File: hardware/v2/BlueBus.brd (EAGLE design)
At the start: 95 x 65 mm, 143 parts, among them J1 3PIN_953442_1, J2 6PIN_953442_1, J3 6PIN_5_103166_1, J4 SJ2-35853A-SMT-TR, J5 SMB_CONN, J6 USB3080-30-01-A, J7 PCM12SMTR, J8 TC2030NL, Q1 NMOSFET-BSS138K, Q2 NMOSFET-BSS138K, Q3 PMOSFET-DMP32D4SSOT323, U1 MPQ4420, U10 PCM5122, U11 PAM8406, U2 TH3122.4, U3 FT231XS, U4 S-1212BC0-U5T1U, U5 XC6210, U6 CAT25M01, U7 PIC24FJ1024GA606, U8 BM83SM1, U9 DIT4096

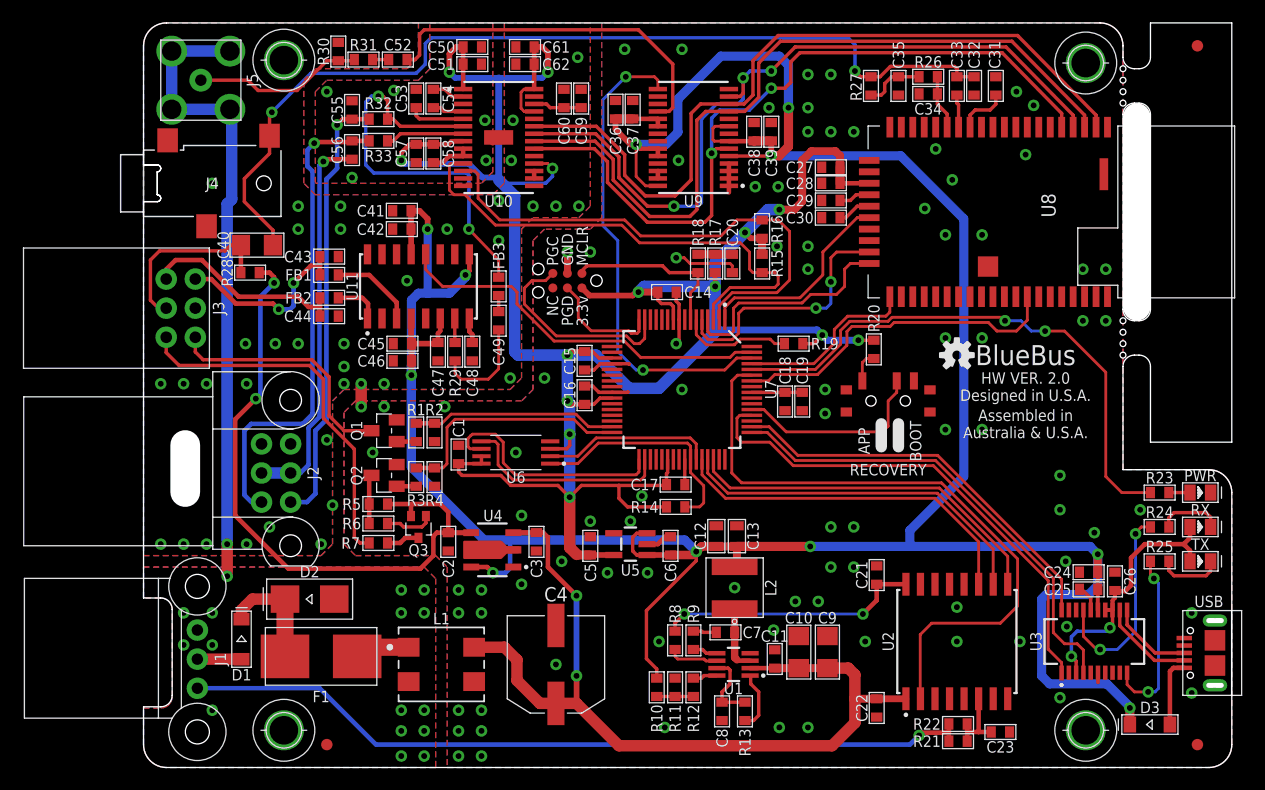
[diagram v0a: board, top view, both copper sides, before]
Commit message: [IMP] hardware: v2 Hardware updates for manufacture * Remove USB cutout * Swap PTH holes to simple holes * Add tCream to USB mount holes
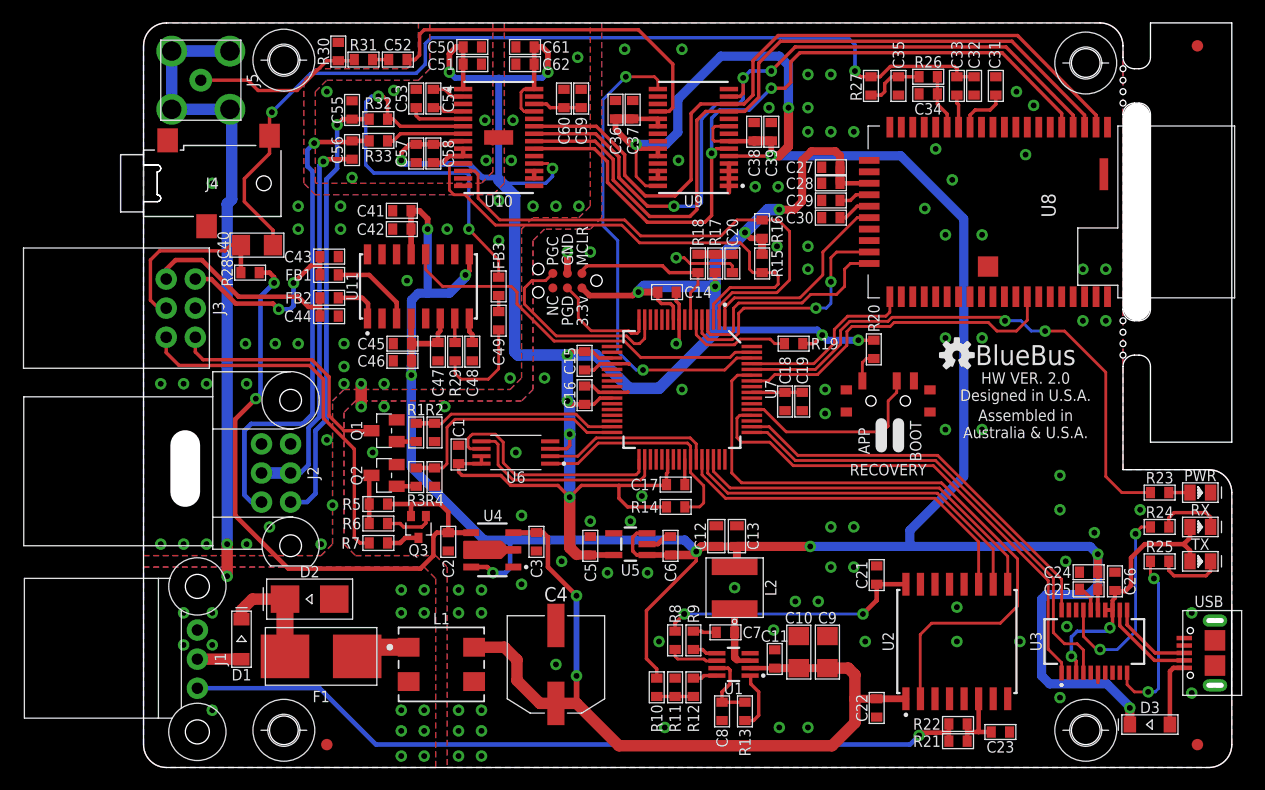
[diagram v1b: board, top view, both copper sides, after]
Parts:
- H1, H2, H3, H4: value 2,5-PAD -> 2,5-HOLE; device Connectors:2.5-PAD -> Connectors:2.5-HOLE
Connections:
- net GND: no longer H2.B2,5, H3.B2,5, H4.B2,5
- net GND_FLT: no longer H1.B2,5
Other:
- outline, holes or cut-outs redrawn
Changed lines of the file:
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@@
 <text x="38.3" y="43.8" size="1" layer="25" font="vector" ratio="15" rot="R90" align="center-left">MCLR</text>
 <text x="37" y="43.8" size="1" layer="25" font="vector" ratio="15" rot="R90" align="center-left">GND</text>
-<wire x1="0" y1="14.8" x2="1.5" y2="14.8" width="0" layer="20"/>
-<wire x1="1.5" y1="14.8" x2="2.5" y2="13.8" width="0" layer="20" curve="-90"/>
-<wire x1="2.5" y1="13.8" x2="2.5" y2="6.3" width="0" layer="20"/>
-<wire x1="2.5" y1="6.3" x2="1.5" y2="5.3" width="0" layer="20" curve="-90"/>
-<wire x1="1.5" y1="5.3" x2="0" y2="5.3" width="0" layer="20"/>
 <wire x1="64.4" y1="30" x2="64.4" y2="28" width="1" layer="25"/>
 <wire x1="65.9" y1="30" x2="65.9" y2="28" width="1" layer="25"/>
@@
 <wire x1="19.85" y1="38.85" x2="5.65" y2="38.85" width="0.1" layer="26"/>
 <wire x1="5.65" y1="41.3" x2="19.85" y2="41.3" width="0.1" layer="26"/>
+<wire x1="0" y1="5.3" x2="0" y2="14.8" width="0" layer="20"/>
 </plain>
 <attributes>
@@
 <attribute name="PN" value="FT231XS-R" x="83" y="11" size="1.778" layer="27" display="off"/>
 </element>
-<element name="H1" library="Connectors" package="2.5-PAD" value="2,5-PAD" x="12.25" y="3.25" smashed="yes"/>
-<element name="H2" library="Connectors" package="2.5-PAD" value="2,5-PAD" x="12.25" y="61.75" smashed="yes"/>
-<element name="H3" library="Connectors" package="2.5-PAD" value="2,5-PAD" x="82.25" y="61.5" smashed="yes"/>
-<element name="H4" library="Connectors" package="2.5-PAD" value="2,5-PAD" x="82.25" y="3.25" smashed="yes"/>
+<element name="H1" library="Connectors" package="2.5-HOLE" value="2,5-HOLE" x="12.25" y="3.25" smashed="yes"/>
+<element name="H2" library="Connectors" package="2.5-HOLE" value="2,5-HOLE" x="12.25" y="61.75" smashed="yes"/>
+<element name="H3" library="Connectors" package="2.5-HOLE" value="2,5-HOLE" x="82.25" y="61.5" smashed="yes"/>
+<element name="H4" library="Connectors" package="2.5-HOLE" value="2,5-HOLE" x="82.25" y="3.25" smashed="yes"/>
 <element name="L2" library="Passives" package="MPL-SE5040" value="10uH" x="51.6" y="15.7" smashed="yes" rot="R270">
 <attribute name="MFG" value="Monolithic Power Systems" x="-10.63" y="-30.02" size="1.778" layer="27" rot="R270" display="off"/>
@@
 <contactref element="C6" pad="2"/>
 <contactref element="J3" pad="4"/>
-<contactref element="H2" pad="B2,5"/>
-<contactref element="H3" pad="B2,5"/>
-<contactref element="H4" pad="B2,5"/>
 <contactref element="C8" pad="2"/>
 <contactref element="C10" pad="2"/>
@@
 <contactref element="J1" pad="1"/>
 <contactref element="L1" pad="2"/>
-<contactref element="H1" pad="B2,5"/>
 <via x="22.5" y="15.5" extent="1-16" drill="0.51"/>
 <via x="24.5" y="15.5" extent="1-16" drill="0.51"/>
@@
 <vertex x="2" y="0" curve="-90"/>
 <vertex x="0" y="2"/>
-<vertex x="0" y="5.2"/>
-<vertex x="1.5" y="5.2" curve="90"/>
-<vertex x="2.5" y="6.2"/>
-<vertex x="2.5" y="13.8" curve="90"/>
-<vertex x="1.5" y="14.8"/>
 <vertex x="0" y="14.8"/>
 <vertex x="0" y="17.5"/>
@@
 <vertex x="2" y="0" curve="-90"/>
 <vertex x="0" y="2"/>
-<vertex x="0" y="5.2"/>
-<vertex x="1.5" y="5.2" curve="90"/>
-<vertex x="2.5" y="6.2"/>
-<vertex x="2.5" y="13.8" curve="90"/>
-<vertex x="1.5" y="14.8"/>
 <vertex x="0" y="14.8"/>
 <vertex x="0" y="17.5"/>

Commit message: [IMP] harcware: Hardware version 2.1 * Swap U4/S-1212BC0 for SOT23-5 package * Update resistor value for R19 to resolve bug with board version identification
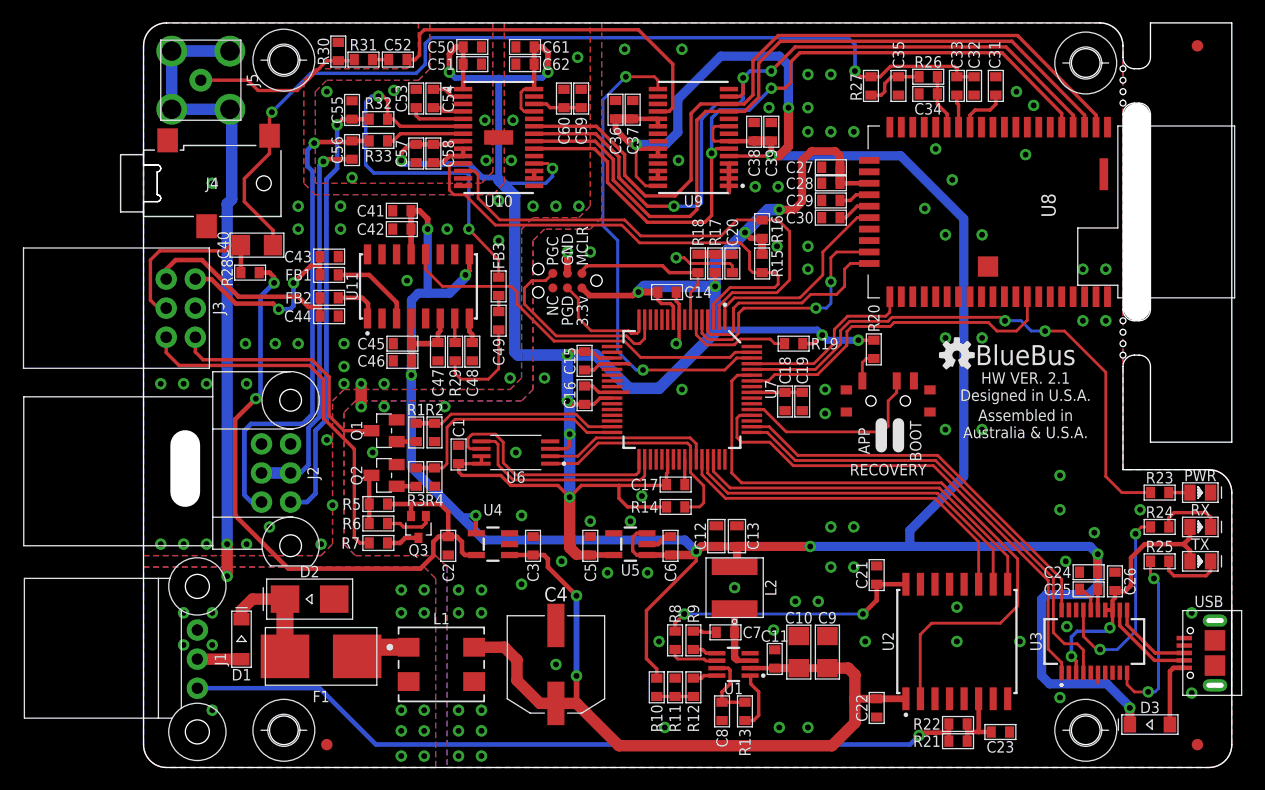
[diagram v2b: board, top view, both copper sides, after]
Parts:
- R19: value 10k -> 100
- U4: value S-1212BC0-U5T1U -> S-1212BC0-M5T1U; device ICs:SOT-89-5 -> ICs:SOT23-5
- moved U4 0.50 mm to (30.5, 19.5)
- moved C3 0.46 mm to (34.0, 19.4), turned to 90 degrees
- moved C2 0.35 mm to (26.6, 19.4)
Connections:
- net 12V: now also U4.5; no longer U4.4
- net 5V: now also U4.4; no longer U4.5
- net VIN: now also U4.1; no longer U4.3
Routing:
- net 5V: track 272.3 -> 269.1 mm
- net VIN: track 75.4 -> 73.9 mm
- net 12V: track 57.0 -> 58.5 mm
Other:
- outline, holes or cut-outs redrawn
- board text added: "HW VER. 2.1"
- board text removed: "HW VER. 2.0"

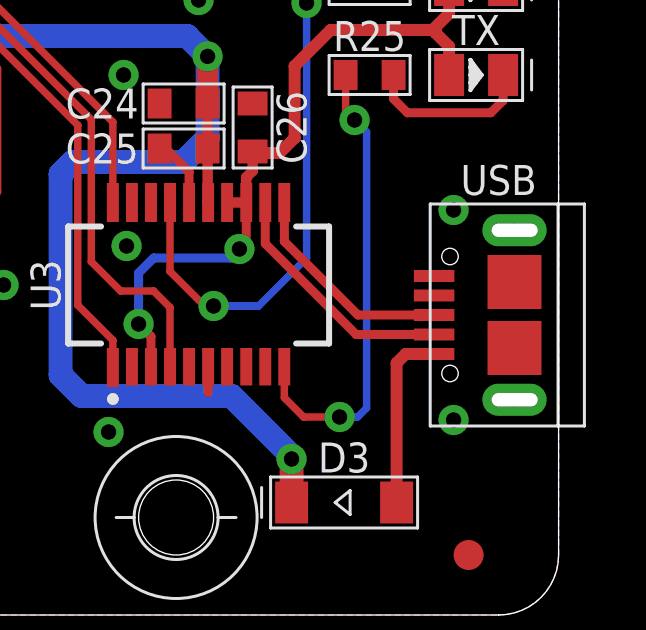
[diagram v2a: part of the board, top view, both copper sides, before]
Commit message: [IMP] hardware: Minor updates to v2.1 * Update EEPROM P/N * Update U6 text layer on PCB * Increase USB port locating pin drill size to 0.65mm to prevent PNP issues
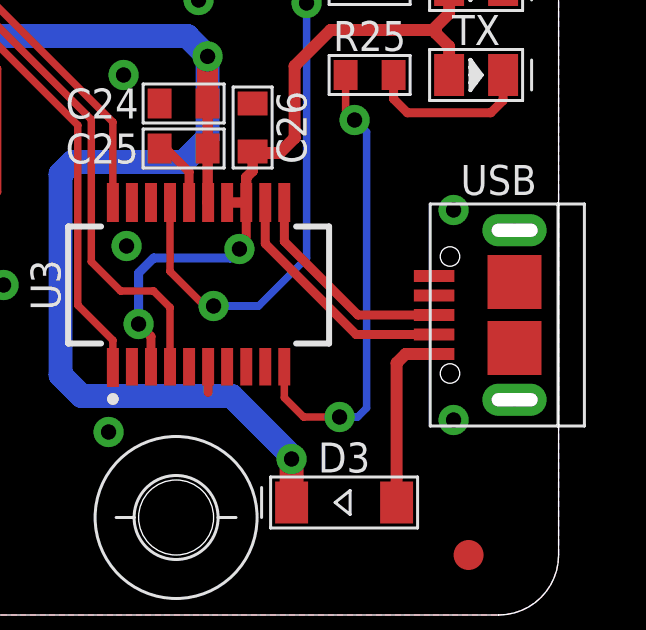
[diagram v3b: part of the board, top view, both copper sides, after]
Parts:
- U6: value CAT25M01 -> CAT25128
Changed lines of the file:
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@@
 <attribute name="PN" value="DIT4096IPW" x="48" y="55" size="1.778" layer="27" rot="R180" display="off"/>
 </element>
-<element name="U6" library="ICs" package="TSSOP-8" value="CAT25M01" x="32.5" y="27.5" smashed="yes" rot="R180">
+<element name="U6" library="ICs" package="TSSOP-8" value="CAT25128" x="32.5" y="27.5" smashed="yes" rot="R180">
 <attribute name="MFG" value="ONSEMI" x="32.5" y="27.5" size="1.778" layer="27" rot="R180" display="off"/>
-<attribute name="NAME" x="32.5" y="25.85" size="1" layer="21" font="vector" ratio="15" rot="R180" align="bottom-center"/>
-<attribute name="PN" value="CAT25M01YI-GT3" x="32.5" y="27.5" size="1.778" layer="27" rot="R180" display="off"/>
+<attribute name="NAME" x="32.5" y="25.85" size="1" layer="25" font="vector" ratio="15" rot="R180" align="bottom-center"/>
+<attribute name="PN" value="CAT25128YI-GT3" x="32.5" y="27.5" size="1.778" layer="27" rot="R180" display="off"/>
 </element>
 <element name="C38" library="Passives" package="0603" value="0.1uF" x="53.3" y="55.5" smashed="yes" rot="R90">

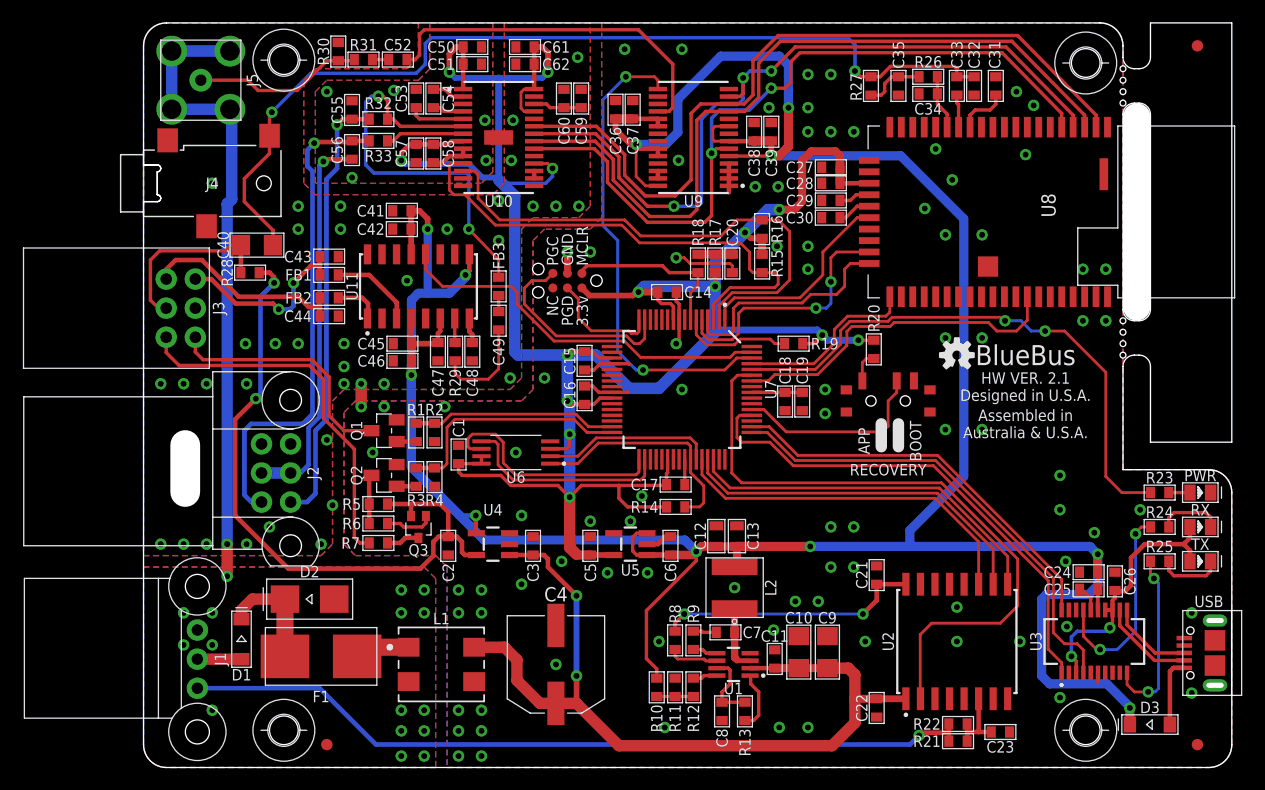
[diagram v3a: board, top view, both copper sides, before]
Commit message: [IMP] firmware: Hardware - Version 2.2 * Add 10k pull-up for I/K-Bus * Add switch to make I/K-Bus pull up optional * Switch R7 to 2k ohms
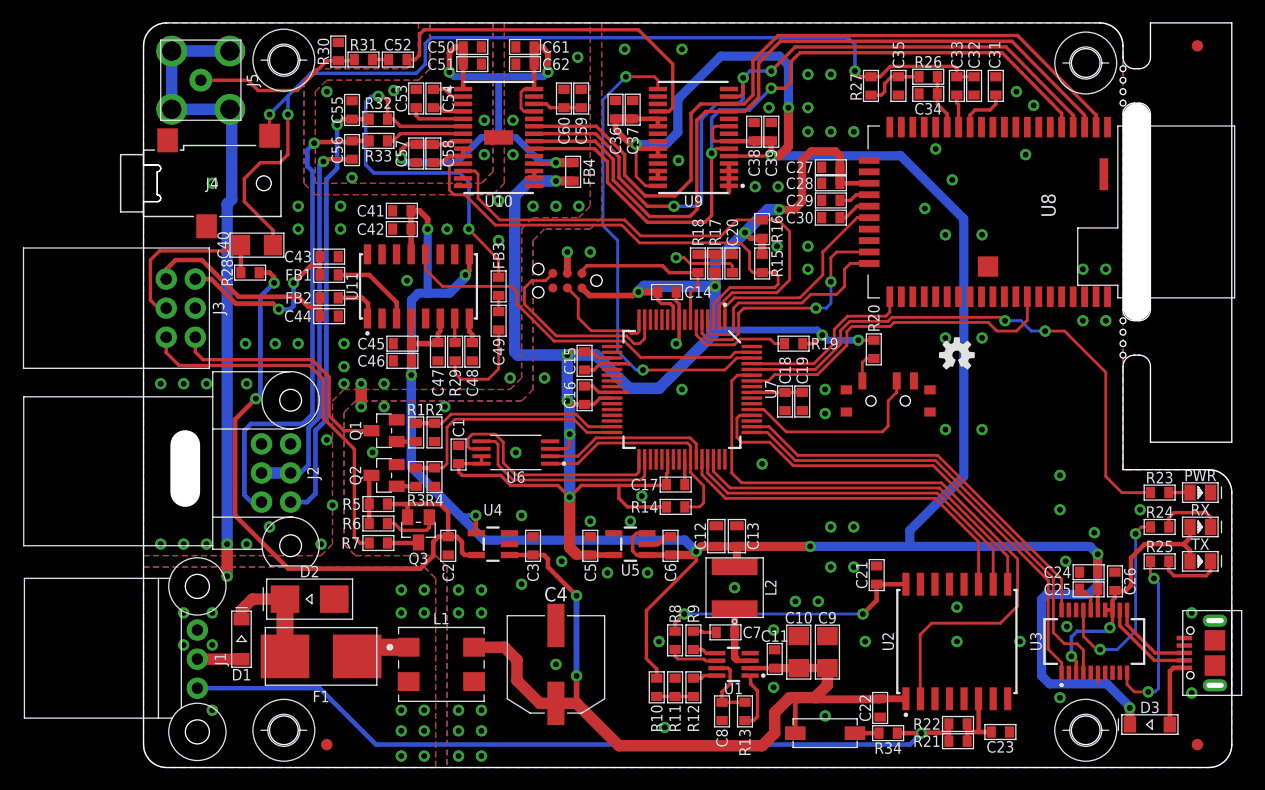
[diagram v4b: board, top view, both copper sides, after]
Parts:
- added FB4: 1A/600OHM, Passives:0603
- added R34: 10k, Passives:0603
- added SW1: CHS-01TA1, Passives:CHS-01TA1
- Q3: value PMOSFET-DMP32D4SSOT323 -> PMOSFET-DMP32D4S; device Passives:SOT323 -> Passives:SOT-23
- R7: value 4.7k -> 2k
- moved C22 0.30 mm to (64.3, 5.20)
- moved Q3 0.25 mm to (24.0, 20.8)
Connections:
- new net DAC_3V3: C50.1, C51.1, C57.1, C58.1, C61.1, C62.1, FB4.2, U10.1, U10.18, U10.25, U10.28, U10.8
- new net IBUS_PU: R34.2, SW1.1
- net 3.3V: now also FB4.1; no longer C50.1, C51.1, C57.1, C58.1, C61.1, C62.1, U10.1, U10.18, U10.25, U10.28, U10.8
- net IBUS: now also R34.1
- net VIN: now also SW1.2
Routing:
- net DAC_3V3: track 0.00 -> 57.1 mm, vias 0 -> 4
- net 3.3V: track 224.5 -> 169.4 mm, vias 14 -> 11
- net BT_MIC_L: track 82.6 -> 87.7 mm, vias 2 -> 3
- net IBUS: track 69.6 -> 71.7 mm
- net IBUS_PU: track 0.00 -> 2.10 mm
- net VIN: track 73.9 -> 75.3 mm
- net TEL_ON_P_RES: track 4.22 -> 4.90 mm
- net GND: vias 124 -> 125
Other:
- board text added: "C1"
- board text added: "C10"
- board text added: "C11"
- board text added: "C12"
- board text added: "C13"
- board text added: "C14"
- board text added: "C15"
- board text added: "C16"
- board text added: "C17"
- board text added: "C18"
- board text added: "C19"
- board text added: "C2"
- board text added: "C20"
- board text added: "C21"
- board text added: "C22"
- board text added: "C23"
- board text added: "C24"
- board text added: "C25"
- board text added: "C26"
- board text added: "C27"
- board text added: "C28"
- board text added: "C29"
- board text added: "C3"
- board text added: "C30"
- board text added: "C31"
- board text added: "C32"
- board text added: "C33"
- board text added: "C34"
- board text added: "C35"
- board text added: "C36"
- board text added: "C37"
- board text added: "C38"
- board text added: "C39"
- board text added: "C4"
- board text added: "C40"
- board text added: "C41"
- board text added: "C42"
- board text added: "C43"
- board text added: "C44"
- board text added: "C45"
- board text added: "C46"
- board text added: "C47"
- board text added: "C48"
- board text added: "C49"
- board text added: "C5"
- board text added: "C50"
- board text added: "C51"
- board text added: "C52"
- board text added: "C53"
- board text added: "C54"
- board text added: "C55"
- board text added: "C56"
- board text added: "C57"
- board text added: "C58"
- board text added: "C59"
- board text added: "C6"
- board text added: "C60"
- board text added: "C61"
- board text added: "C62"
- board text added: "C7"
- board text added: "C8"
- board text added: "C9"
- board text added: "D1"
- board text added: "D2"
- board text added: "D3"
- board text added: "F1"
- board text added: "FB1"
- board text added: "FB2"
- board text added: "FB3"
- board text added: "FB4"
- board text added: "HW VER. 2.2"
- board text added: "I/K-BUS PULL UP"
- board text added: "J1"
- board text added: "J2"
- board text added: "J3"
- board text added: "J4"
- board text added: "J5"
- board text added: "L1"
- board text added: "L2"
- board text added: "PWR"
- board text added: "Q1"
- board text added: "Q2"
- board text added: "Q3"
- board text added: "R1"
- board text added: "R10"
- board text added: "R11"
- board text added: "R12"
- board text added: "R13"
- board text added: "R14"
- board text added: "R15"
- board text added: "R16"
- board text added: "R17"
- board text added: "R18"
- board text added: "R19"
- board text added: "R2"
- board text added: "R20"
- board text added: "R21"
- board text added: "R22"
- board text added: "R23"
- board text added: "R24"
- board text added: "R25"
- board text added: "R26"
- board text added: "R27"
- board text added: "R28"
- board text added: "R29"
- board text added: "R3"
- board text added: "R30"
- board text added: "R31"
- board text added: "R32"
- board text added: "R33"
- board text added: "R34"
- board text added: "R4"
- board text added: "R5"
- board text added: "R6"
- board text added: "R7"
- board text added: "R8"
- board text added: "R9"
- board text added: "RX"
- board text added: "TX"
- board text added: "U1"
- board text added: "U10"
- board text added: "U11"
- board text added: "U2"
- board text added: "U3"
- board text added: "U4"
- board text added: "U5"
- board text added: "U6"
- board text added: "U7"
- board text added: "U8"
- board text added: "U9"
- board text removed: "HW VER. 2.1"
